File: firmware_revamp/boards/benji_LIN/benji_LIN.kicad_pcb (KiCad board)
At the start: 2 copper layers, 109.3 x 58.3 mm, 19 parts, among them U101 TPS560430YF

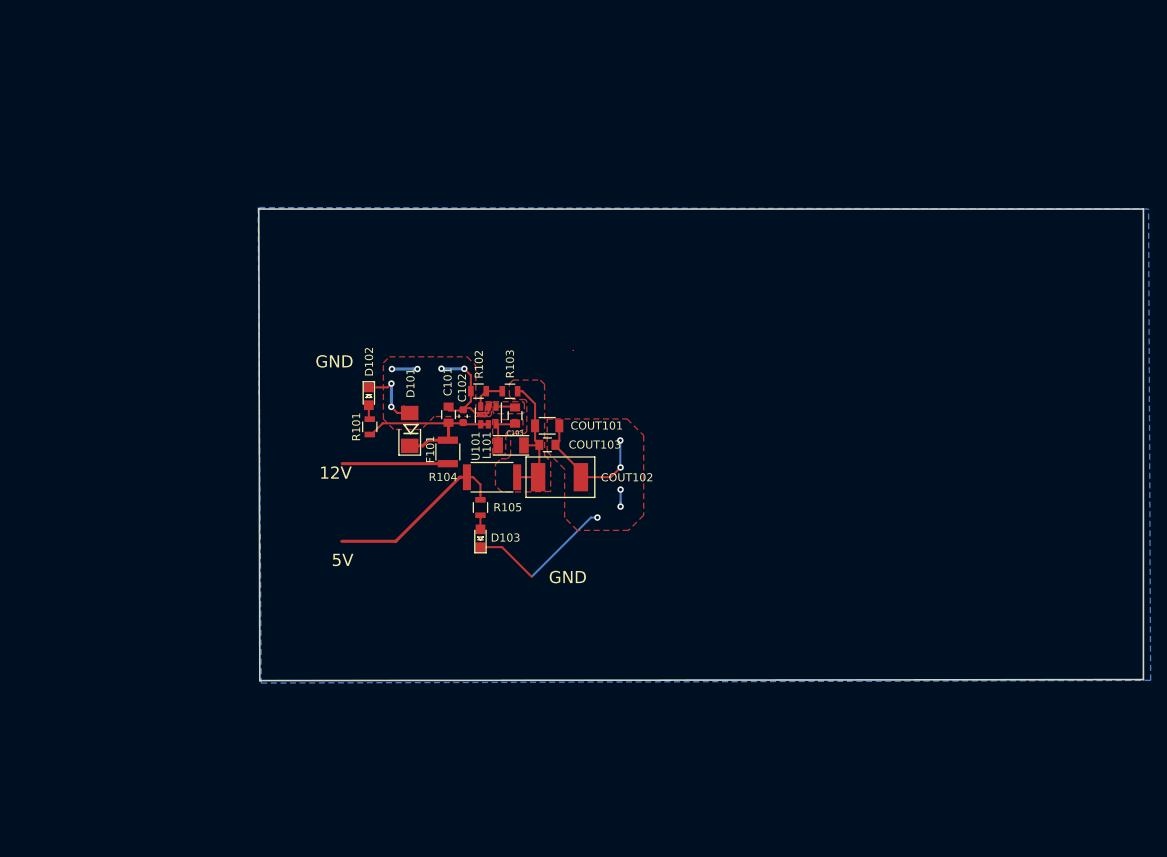
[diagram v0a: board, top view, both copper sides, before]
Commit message: Fixed switch ground, first pass of layout
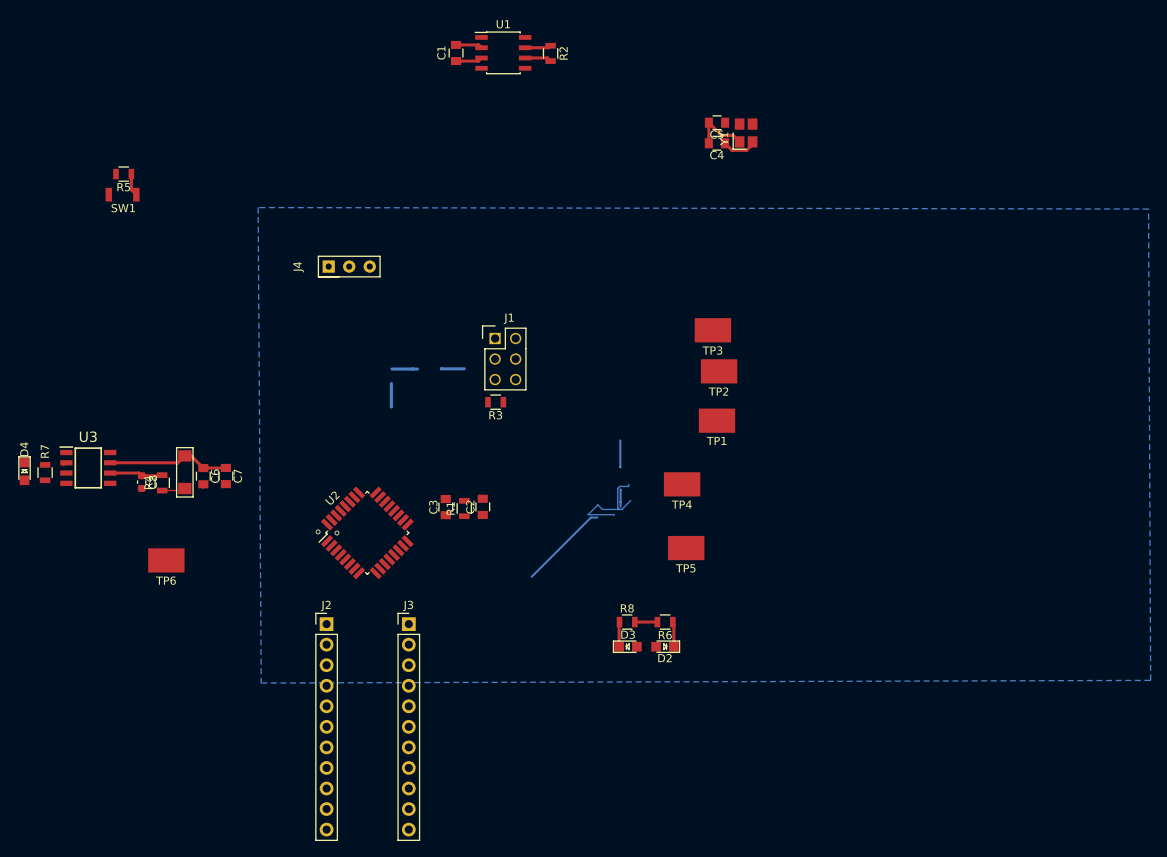
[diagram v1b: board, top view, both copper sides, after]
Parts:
- removed C101, C103: C_0.1uF, footprints:C_0805_OEM
- removed C102: C_2.2uF, footprints:C_0603_1608Metric
- removed COUT101: C_22uF, footprints:C_1206_OEM
- removed COUT102: C_33uF, footprints:Fuse_1812
- removed COUT103: C_47uF, footprints:C_0805_OEM
- removed D101: D_Zener_18V, footprints:DO-214AA
- removed D102, D103: LED_0805, footprints:LED_0805_OEM
- removed F101: F_500mA_16V, footprints:Fuse_1210
- removed G***: LOGO, footprints:Logo_Large
- removed G***: LOGO, footprints:phoenix
- removed L101: L_100uH, footprints:L_100uH_OEM
- removed R101: R_1K, footprints:R_0805_OEM
- removed R102: R_25K, footprints:R_0805_OEM
- removed R103: R_100K, footprints:R_0805_OEM
- removed R104: R_0_2512, footprints:R_2512_OEM
- removed R105: R_200, footprints:R_0805_OEM
- removed U101: TPS560430YF, footprints:SOT-23-6_OEM
- added C1: C_0.1uF, footprints:C_0805_OEM, F.Cu at (122.7, 57.2)
- added C2: C_0.1uF, footprints:C_0805_OEM, F.Cu at (126.0, 113.3)
- added C3: C_100pF, footprints:C_0805_OEM, F.Cu at (121.4, 113.3)
- added C4: C_30pF, footprints:C_0805_OEM, F.Cu at (154.9, 68.3)
- added C5: C_30pF, footprints:C_0805_OEM, F.Cu at (154.9, 65.8)
- added C6: C_0.1uF, footprints:C_0805_OEM, F.Cu at (91.4, 109.5)
- added C7: C_0.1uF, footprints:C_0805_OEM, F.Cu at (94.2, 109.5)
- added C8: C_220pF, footprints:C_0603_1608Metric, F.Cu at (83.8, 110.2)
- added D1: Diode_600V_1A_SM, footprints:Diode_600V_1A_SM, F.Cu at (89.2, 107.0)
- added D2: LED_0805, footprints:LED_0805_OEM, F.Cu at (148.5, 130.6)
- added D3: LED_0805_Red, footprints:LED_0805_OEM, F.Cu at (143.9, 130.6)
- added D4: LIN_INDICATOR_LED, footprints:LED_0805_OEM, F.Cu at (69.3, 108.9)
- added J1: CONN_02X03, footprints:Pin_Header_Straight_2x03, F.Cu at (127.5, 92.5)
- added J2: Conn_01x11, footprints:PinHeader_1x11_P2.54mm_Vertical, F.Cu at (106.7, 127.8)
- added J3: Conn_01x11, footprints:PinHeader_1x11_P2.54mm_Vertical, F.Cu at (116.8, 127.8)
- added J4: CONN_01X03, footprints:PinHeader_1x03_P2.54mm_Vertical, F.Cu at (106.9, 83.6)
- added R1: R_100, footprints:R_0805_OEM, F.Cu at (123.7, 113.5)
- added R2: R_120_DNP, footprints:R_0805_OEM, F.Cu at (134.4, 57.2)
- added R3: R_10K, footprints:R_0805_OEM, F.Cu at (127.6, 100.3)
- added R4: R_1K, footprints:R_0805_OEM, F.Cu at (86.4, 110.3)
- added R5: R_1K, footprints:R_0805_OEM, F.Cu at (81.6, 72.1)
- added R6: R_1K, footprints:R_0805_OEM, F.Cu at (148.5, 127.5)
- added R7: R_1K, footprints:R_0805_OEM, F.Cu at (71.9, 109.0)
- added R8: R_1K, footprints:R_0805_OEM, F.Cu at (143.8, 127.5)
- added SW1: SW_Push_SPST_NO, footprints:SW_B3U-1000P_4.2x1.7mm, F.Cu at (83.2, 74.7)
- added TP1: Test_Point_SMD, footprints:Test_Point_SMD, F.Cu at (154.9, 102.6)
- added TP2: Test_Point_SMD, footprints:Test_Point_SMD, F.Cu at (155.2, 96.5)
- added TP3: Test_Point_SMD, footprints:Test_Point_SMD, F.Cu at (154.4, 91.4)
- added TP4: Test_Point_SMD, footprints:Test_Point_SMD, F.Cu at (150.6, 110.5)
- added TP5: Test_Point_SMD, footprints:Test_Point_SMD, F.Cu at (151.1, 118.4)
- added TP6: Test_Point_SMD, footprints:Test_Point_SMD, F.Cu at (86.9, 119.9)
- added U1: MCP2561-E_SN, footprints:SOIC-8_3.9x4.9mm_Pitch1.27mm_OEM, F.Cu at (128.5, 57.1)
- added U2: ATMEGA16M1, footprints:TQFP-32_7x7mm_Pitch0.8mm, F.Cu at (111.7, 116.5)
- added U3: TLIN1021DRQ1, footprints:SOIC127P600X175-8N, F.Cu at (77.2, 108.5)
- added Y1: Crystal_SMD, footprints:Crystal_SMD_FA238, F.Cu at (158.5, 67.1)
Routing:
- net GND: track 65.5 -> 28.1 mm, vias 11 -> 0
- net Net-(J2-Pad9): track 0.00 -> 25.6 mm
- net Net-(C101-Pad1): track 22.9 -> 0.00 mm
- net VCC: track 22.7 -> 3.30 mm
- net Net-(COUT101-Pad1): track 17.3 -> 0.00 mm
- net /VIN: track 0.00 -> 15.7 mm
- net /12V: track 13.1 -> 0.00 mm
- net /LIN_BUS: track 0.00 -> 6.70 mm
- net Net-(C103-Pad2): track 5.44 -> 0.00 mm
- net Net-(C4-Pad1): track 0.00 -> 4.39 mm
- net Net-(R102-Pad1): track 4.18 -> 0.00 mm
- net /CAN_-: track 0.00 -> 3.30 mm
- net /CAN_+: track 0.00 -> 3.25 mm
- net Net-(D3-Pad1): track 0.00 -> 3.07 mm
- net Net-(D2-Pad1): track 0.00 -> 2.79 mm
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- removed copper zone on F.Cu, net GND
- removed copper zone on F.Cu, net Net-(C103-Pad1)
- removed copper zone on F.Cu, net Net-(C103-Pad2)
- removed copper zone on F.Cu, net Net-(COUT101-Pad1)
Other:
- board outline removed
- board text removed: "12V"
- board text removed: "5V"
- board text removed: "GND"
